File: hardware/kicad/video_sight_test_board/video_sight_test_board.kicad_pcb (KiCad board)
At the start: 2 copper layers, 53 parts, among them J1 BATTERY, J2 XIAO_BREAKOUT_BOARD, J3 LCD, J4 BNO055_MODULE, J5 UPDI, J6 ATtiny1616_LEFT, J7 ATtiny1616_RIGHT, J8 INPUT_DEVICE, Q1 AO3401A, SW1 SW_BATT, SW2 WAKE, SW3 UP, SW4 DOWN, SW5 FRONT, SW6 BACK, SW7 RotaryEncoder, U1 TPS22919, U2 ATTINY1616-SN

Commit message: PCBざっくり置いた
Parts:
- J2: value XIAO_BREAKOUT_BOARD -> XIAO
- TP10: value SPI_MISO -> MISO
- TP13: value IMU_2V8_OUT -> 2V8_OUT
- TP15: value IMU_INT -> INT
- TP16: value IMU_RESET -> RESET
- TP5: value XIAO_3V3 -> 3V3
- TP6: value PERIPH_EN -> EN
- moved C8 123.7 mm to (234.9, 136.8), turned to -90 degrees
- moved R6 120.7 mm to (229.9, 126.1), turned to -90 degrees
- moved R8 104.1 mm to (213.4, 129.5), turned to 180 degrees
- moved R7 103.8 mm to (213.4, 125.6), turned to 180 degrees
- moved C5 92.4 mm to (209.3, 84.5)
- moved R3 91.6 mm to (201.7, 109.9), turned to 180 degrees
- moved C6 90.0 mm to (202.8, 120.7)
- moved TP5 89.3 mm to (214.6, 68.6)
- moved TP13 88.9 mm to (207.6, 137.2)
- moved C2 87.0 mm to (201.7, 107.3), turned to 180 degrees
- moved C7 86.9 mm to (203.6, 88.3), turned to 180 degrees
- moved R2 85.9 mm to (197.6, 97.2), turned to 180 degrees
- moved C1 85.6 mm to (201.7, 97.2), turned to 180 degrees
- moved TP6 85.2 mm to (209.6, 68.6)
- moved TP12 85.0 mm to (213.4, 117.5)
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- renumbered TP2 to TP1, TP1 to TP2
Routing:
- net /I2C_SCL: track 0.00 -> 136.6 mm
- net /I2C_SDA: track 0.00 -> 126.9 mm
- net PERIPH_3V3: track 0.00 -> 97.6 mm
- net /WAKE: track 0.00 -> 66.6 mm
- net Net-(J8-Pin_4): track 0.00 -> 57.8 mm
- net Net-(J8-Pin_1): track 0.00 -> 55.6 mm
- net Net-(J8-Pin_3): track 0.00 -> 47.6 mm
- net XIAO_3V3: track 0.00 -> 47.1 mm
- net +BATT: track 0.00 -> 44.6 mm
- net /PERIPH_EN: track 0.00 -> 40.7 mm, vias 0 -> 1
- net Net-(J8-Pin_2): track 0.00 -> 40.2 mm
- net /PA0_UPDI: track 0.00 -> 21.1 mm
- net UPDI_VCC: track 0.00 -> 18.6 mm
- net Net-(J1-Pin_1): track 0.00 -> 18.0 mm
- net Net-(Q1-D): track 0.00 -> 16.0 mm
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- added copper zone on B.Cu, net GND
- added copper zone on F.Cu, net GND
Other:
- board outline added: 99.1 x 99.1 mm

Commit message: テストボードPCBだいたい完成
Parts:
- added ?: , , F.Cu at (224.2, 97.8)
- added ?: , , F.Cu at (222.9, 154.3)
- added ?: , , F.Cu at (181.0, 154.3)
- added ?: , , F.Cu at (229.2, 100.3)
- added ?: , , F.Cu at (214.0, 144.1)
- added ?: , , F.Cu at (211.5, 146.7)
- added ?: , , F.Cu at (250.8, 159.4)
- added ?: , , F.Cu at (224.2, 105.4)
- added ?: , , F.Cu at (191.1, 151.8)
- added ?: , , F.Cu at (191.1, 146.7)
- added ?: , , F.Cu at (208.9, 144.1)
- added ?: , , F.Cu at (206.4, 146.7)
- added ?: , , F.Cu at (193.7, 149.2)
- added ?: , , F.Cu at (221.6, 100.3)
- added ?: , , F.Cu at (229.2, 95.2)
- added ?: , , F.Cu at (250.8, 154.3)
- added ?: , , F.Cu at (240.7, 151.8)
- added ?: , , F.Cu at (224.2, 100.3)
- added ?: , , F.Cu at (214.0, 151.8)
- added ?: , , F.Cu at (208.9, 146.7)
- added ?: , , F.Cu at (226.7, 100.3)
- added ?: , , F.Cu at (178.4, 149.2)
- added ?: , , F.Cu at (226.7, 92.7)
- added ?: , , F.Cu at (225.4, 151.8)
- added ?: , , F.Cu at (255.9, 156.8)
- added ?: , , F.Cu at (181.0, 144.1)
- added ?: , , F.Cu at (221.6, 97.8)
- added ?: , , F.Cu at (181.0, 156.8)
- added ?: , , F.Cu at (183.5, 156.8)
- added ?: , , F.Cu at (193.7, 144.1)
- added ?: , , F.Cu at (214.0, 159.4)
- added ?: , , F.Cu at (229.2, 105.4)
- added ?: , , F.Cu at (183.5, 151.8)
- added ?: , , F.Cu at (211.5, 154.3)
- added ?: , , F.Cu at (255.9, 151.8)
- added ?: , , F.Cu at (203.8, 149.2)
- added ?: , , F.Cu at (248.3, 156.8)
- added ?: , , F.Cu at (233.0, 154.3)
- added ?: , , F.Cu at (196.2, 151.8)
- added ?: , , F.Cu at (203.8, 156.8)
- added ?: , , F.Cu at (186.1, 146.7)
- added ?: , , F.Cu at (183.5, 149.2)
- added ?: , , F.Cu at (253.4, 159.4)
- added ?: , , F.Cu at (186.1, 154.3)
- added ?: , , F.Cu at (258.4, 159.4)
- added ?: , , F.Cu at (183.5, 154.3)
- added ?: , , F.Cu at (238.1, 156.8)
- added ?: , , F.Cu at (211.5, 149.2)
- added ?: , , F.Cu at (188.6, 149.2)
- added ?: , , F.Cu at (243.2, 159.4)
- added ?: , , F.Cu at (201.3, 154.3)
- added ?: , , F.Cu at (203.8, 146.7)
- added ?: , , F.Cu at (243.2, 156.8)
- added ?: , , F.Cu at (222.9, 151.8)
- added ?: , , F.Cu at (228.0, 151.8)
- added ?: , , F.Cu at (243.2, 151.8)
- added ?: , , F.Cu at (230.5, 151.8)
- added ?: , , F.Cu at (225.4, 154.3)
- added ?: , , F.Cu at (245.7, 156.8)
- added ?: , , F.Cu at (196.2, 156.8)
- added ?: , , F.Cu at (248.3, 151.8)
- added ?: , , F.Cu at (214.0, 156.8)
- added ?: , , F.Cu at (224.2, 92.7)
- added ?: , , F.Cu at (193.7, 154.3)
- added ?: , , F.Cu at (178.4, 144.1)
- added ?: , , F.Cu at (230.5, 159.4)
- added ?: , , F.Cu at (224.2, 95.2)
- added ?: , , F.Cu at (191.1, 144.1)
- added ?: , , F.Cu at (193.7, 146.7)
- added ?: , , F.Cu at (211.5, 151.8)
- added ?: , , F.Cu at (193.7, 159.4)
- added ?: , , F.Cu at (188.6, 156.8)
- added ?: , , F.Cu at (186.1, 151.8)
- added ?: , , F.Cu at (201.3, 156.8)
- added ?: , , F.Cu at (211.5, 144.1)
- added ?: , , F.Cu at (226.7, 105.4)
- added ?: , , F.Cu at (255.9, 154.3)
- added ?: , , F.Cu at (206.4, 154.3)
- added ?: , , F.Cu at (245.7, 151.8)
- added ?: , , F.Cu at (250.8, 156.8)
- added ?: , , F.Cu at (225.4, 156.8)
- added ?: , , F.Cu at (253.4, 156.8)
- added ?: , , F.Cu at (198.8, 149.2)
- added ?: , , F.Cu at (198.8, 146.7)
- added ?: , , F.Cu at (229.2, 108.0)
- added ?: , , F.Cu at (208.9, 159.4)
- added ?: , , F.Cu at (229.2, 92.7)
- added ?: , , F.Cu at (186.1, 156.8)
- added ?: , , F.Cu at (188.6, 151.8)
- added ?: , , F.Cu at (178.4, 154.3)
- added ?: , , F.Cu at (186.1, 144.1)
- added ?: , , F.Cu at (201.3, 159.4)
- added ?: , , F.Cu at (253.4, 154.3)
- added ?: , , F.Cu at (181.0, 151.8)
- added ?: , , F.Cu at (193.7, 156.8)
- added ?: , , F.Cu at (181.0, 146.7)
- added ?: , , F.Cu at (201.3, 151.8)
- added ?: , , F.Cu at (181.0, 159.4)
- added ?: , , F.Cu at (191.1, 154.3)
- added ?: , , F.Cu at (191.1, 159.4)
- added ?: , , F.Cu at (211.5, 159.4)
- added ?: , , F.Cu at (230.5, 156.8)
- added ?: , , F.Cu at (178.4, 151.8)
- added ?: , , F.Cu at (203.8, 159.4)
- added ?: , , F.Cu at (226.7, 108.0)
- added ?: , , F.Cu at (240.7, 156.8)
- added ?: , , F.Cu at (245.7, 159.4)
- added ?: , , F.Cu at (206.4, 159.4)
- added ?: , , F.Cu at (208.9, 154.3)
- added ?: , , F.Cu at (198.8, 159.4)
- added ?: , , F.Cu at (178.4, 156.8)
- added ?: , , F.Cu at (196.2, 159.4)
- added ?: , , F.Cu at (238.1, 159.4)
- added ?: , , F.Cu at (203.8, 144.1)
- added ?: , , F.Cu at (188.6, 154.3)
- added ?: , , F.Cu at (206.4, 156.8)
- added ?: , , F.Cu at (183.5, 159.4)
- added ?: , , F.Cu at (245.7, 154.3)
- added ?: , , F.Cu at (238.1, 151.8)
- added ?: , , F.Cu at (211.5, 156.8)
- added ?: , , F.Cu at (201.3, 149.2)
- added ?: , , F.Cu at (225.4, 159.4)
- added ?: , , F.Cu at (235.6, 156.8)
- added ?: , , F.Cu at (221.6, 95.2)
- added ?: , , F.Cu at (203.8, 151.8)
- added ?: , , F.Cu at (228.0, 159.4)
- added ?: , , F.Cu at (224.2, 108.0)
- added ?: , , F.Cu at (188.6, 146.7)
- added ?: , , F.Cu at (229.2, 97.8)
- added ?: , , F.Cu at (229.2, 102.9)
- added ?: , , F.Cu at (248.3, 154.3)
- added ?: , , F.Cu at (243.2, 154.3)
- added ?: , , F.Cu at (193.7, 151.8)
- added ?: , , F.Cu at (226.7, 97.8)
- added ?: , , F.Cu at (186.1, 159.4)
- added ?: , , F.Cu at (221.6, 92.7)
- added ?: , , F.Cu at (250.8, 151.8)
- added ?: , , F.Cu at (233.0, 159.4)
- added ?: , , F.Cu at (235.6, 154.3)
- added ?: , , F.Cu at (255.9, 159.4)
- added ?: , , F.Cu at (258.4, 154.3)
- added ?: , , F.Cu at (198.8, 156.8)
- added ?: , , F.Cu at (208.9, 156.8)
- added ?: , , F.Cu at (253.4, 151.8)
- added ?: , , F.Cu at (196.2, 154.3)
- added ?: , , F.Cu at (208.9, 151.8)
- added ?: , , F.Cu at (183.5, 146.7)
- added ?: , , F.Cu at (196.2, 146.7)
- added ?: , , F.Cu at (258.4, 151.8)
- added ?: , , F.Cu at (201.3, 146.7)
- added ?: , , F.Cu at (221.6, 108.0)
- added ?: , , F.Cu at (203.8, 154.3)
- added ?: , , F.Cu at (196.2, 149.2)
- added ?: , , F.Cu at (258.4, 156.8)
- added ?: , , F.Cu at (214.0, 146.7)
- added ?: , , F.Cu at (201.3, 144.1)
- added ?: , , F.Cu at (186.1, 149.2)
- added ?: , , F.Cu at (240.7, 159.4)
- added ?: , , F.Cu at (178.4, 146.7)
- added ?: , , F.Cu at (233.0, 156.8)
- added ?: , , F.Cu at (183.5, 144.1)
- added ?: , , F.Cu at (191.1, 149.2)
- added ?: , , F.Cu at (230.5, 154.3)
- added ?: , , F.Cu at (222.9, 156.8)
- added ?: , , F.Cu at (228.0, 156.8)
- added ?: , , F.Cu at (228.0, 154.3)
- added ?: , , F.Cu at (238.1, 154.3)
- added ?: , , F.Cu at (240.7, 154.3)
- added ?: , , F.Cu at (235.6, 159.4)
- added ?: , , F.Cu at (191.1, 156.8)
- added ?: , , F.Cu at (206.4, 144.1)
- added ?: , , F.Cu at (198.8, 151.8)
- added ?: , , F.Cu at (188.6, 144.1)
- added ?: , , F.Cu at (208.9, 149.2)
- added ?: , , F.Cu at (214.0, 149.2)
- added ?: , , F.Cu at (198.8, 154.3)
- added ?: , , F.Cu at (221.6, 102.9)
- added ?: , , F.Cu at (221.6, 105.4)
- added ?: , , F.Cu at (178.4, 159.4)
- added ?: , , F.Cu at (188.6, 159.4)
- added ?: , , F.Cu at (226.7, 95.2)
- added ?: , , F.Cu at (226.7, 102.9)
- added ?: , , F.Cu at (198.8, 144.1)
- added ?: , , F.Cu at (222.9, 159.4)
- added ?: , , F.Cu at (233.0, 151.8)
- added ?: , , F.Cu at (248.3, 159.4)
- added ?: , , F.Cu at (206.4, 151.8)
- added ?: , , F.Cu at (214.0, 154.3)
- added ?: , , F.Cu at (196.2, 144.1)
- added ?: , , F.Cu at (224.2, 102.9)
- added ?: , , F.Cu at (206.4, 149.2)
- added ?: , , F.Cu at (235.6, 151.8)
- added ?: , , F.Cu at (181.0, 149.2)
- added REF**: MountingHole_3.2mm_M3, MountingHole:MountingHole_3.2mm_M3, F.Cu at (264.2, 159.4)
- added REF**: MountingHole_3.2mm_M3, MountingHole:MountingHole_3.2mm_M3, F.Cu at (172.7, 67.9)
- added REF**: MountingHole_3.2mm_M3, MountingHole:MountingHole_3.2mm_M3, F.Cu at (172.7, 159.4)
- added REF**: MountingHole_3.2mm_M3, MountingHole:MountingHole_3.2mm_M3, F.Cu at (264.2, 67.9)
- J4: value BNO055_MODULE -> BNO055
- moved TP11 12.8 mm to (212.1, 123.8)
- moved R7 4.08 mm to (214.3, 129.5)
- moved R8 2.11 mm to (214.3, 131.4)
- moved C9 1.27 mm to (184.8, 69.2)
- moved R4 1.27 mm to (179.7, 69.2)
- moved R5 1.27 mm to (182.2, 69.2)
- moved TP12 1.27 mm to (212.1, 117.5)
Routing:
- net PERIPH_3V3: track 97.6 -> 103.5 mm
- net /I2C_SCL: track 136.6 -> 140.8 mm
- net Net-(J1-Pin_1): track 18.0 -> 21.7 mm
- net /I2C_SDA: track 126.9 -> 130.2 mm
- net Net-(J8-Pin_4): track 57.8 -> 60.4 mm
- net XIAO_3V3: track 47.1 -> 46.1 mm
- net /PERIPH_EN: track 40.7 -> 41.8 mm
- net /BATT_ADC: track 11.6 -> 11.0 mm
- net GND: vias 2 -> 71
- net (no net): vias 0 -> 1
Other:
- board text added: "GND"
- board text added: "PA0"
- board text added: "PA1"
- board text added: "PA2"
- board text added: "PA3"
- board text added: "PA4"
- board text added: "PA5"
- board text added: "PA6"
- board text added: "PA7"
- board text added: "PB2"
- board text added: "PB3"
- board text added: "PB4"
- board text added: "PB5"
- board text added: "PC0"
- board text added: "PC1"
- board text added: "PC2"
- board text added: "PC3"
- board text added: "VCC"
- board text added: "VIDEO_SIGHT_TEST_BOARD Rev.1"

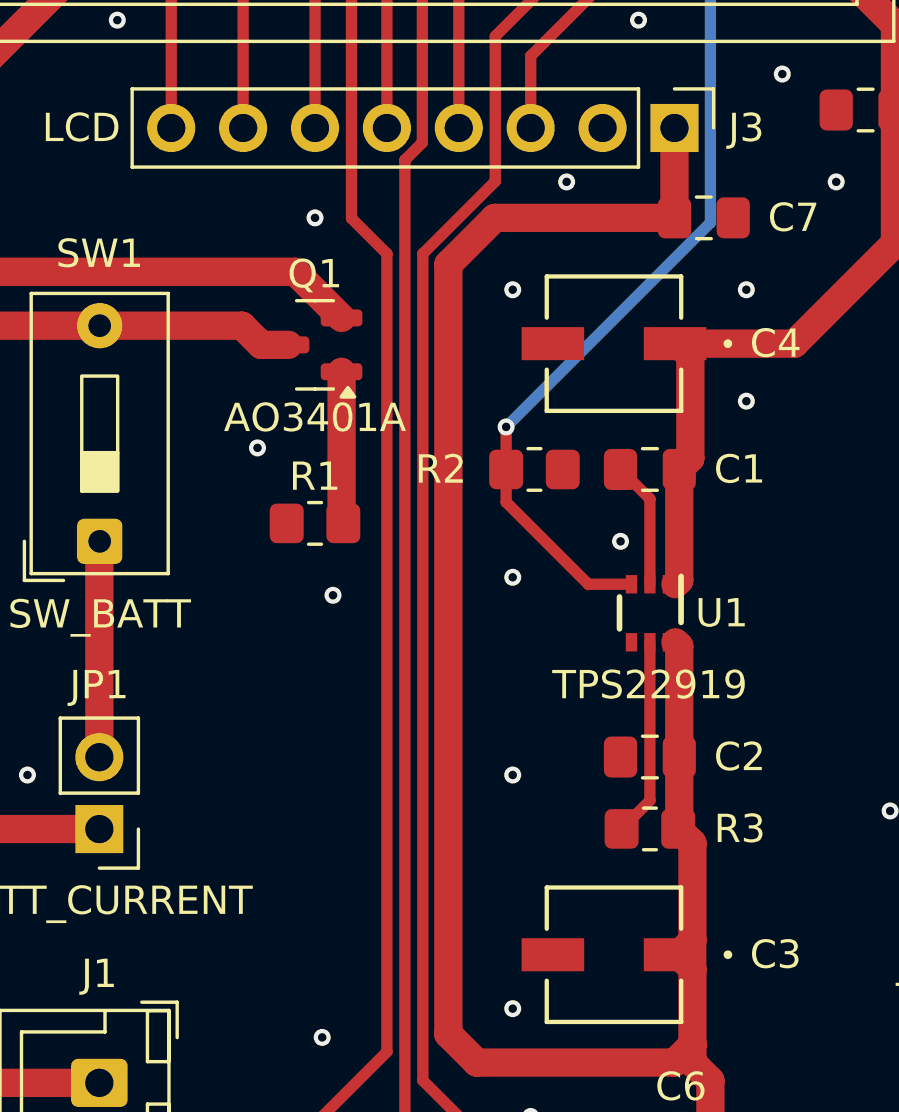
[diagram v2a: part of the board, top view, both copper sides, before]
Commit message: シルク追加
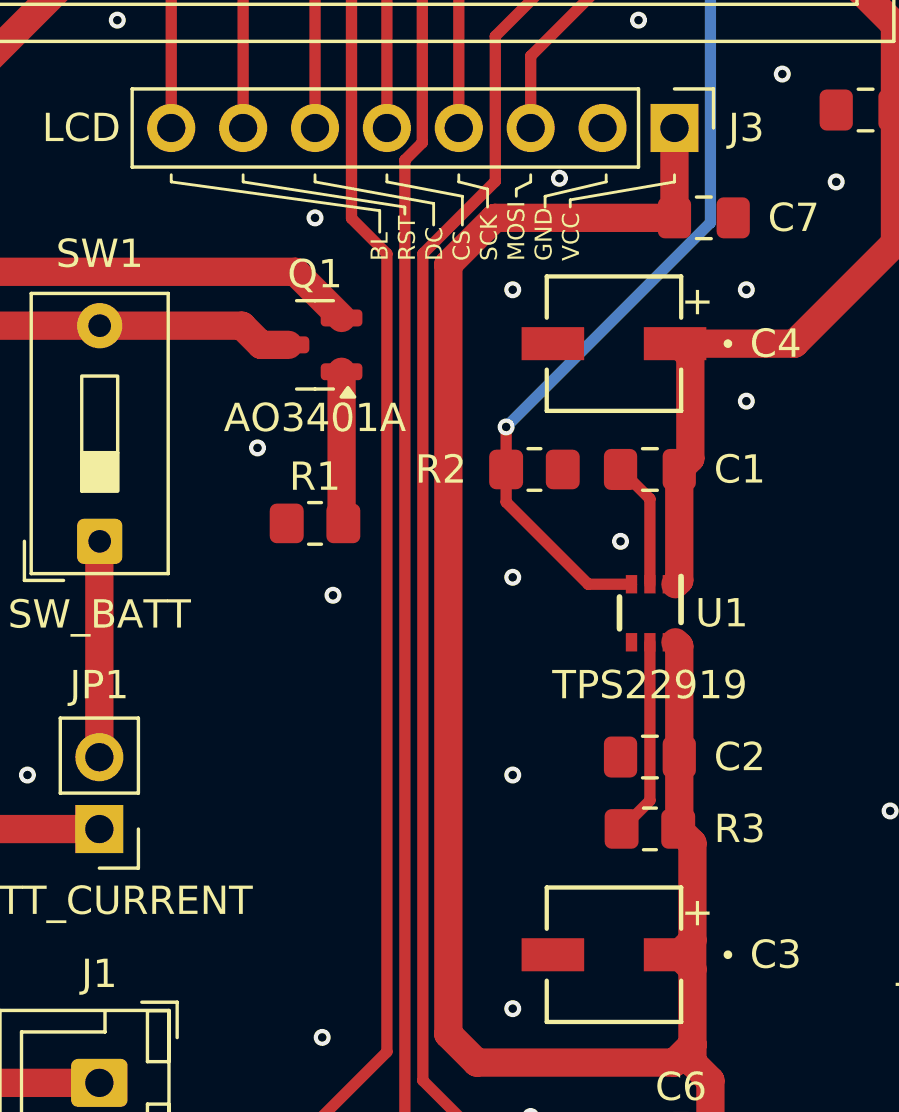
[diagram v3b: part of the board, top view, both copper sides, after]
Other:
- board text added: "+"
- board text added: "BL RST DC CS SCK MOSI GND VCC"
